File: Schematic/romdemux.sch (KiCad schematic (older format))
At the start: 14 parts, among them SW10 SW_Push, U10 27C020, U11 74LS154, U12 NE555

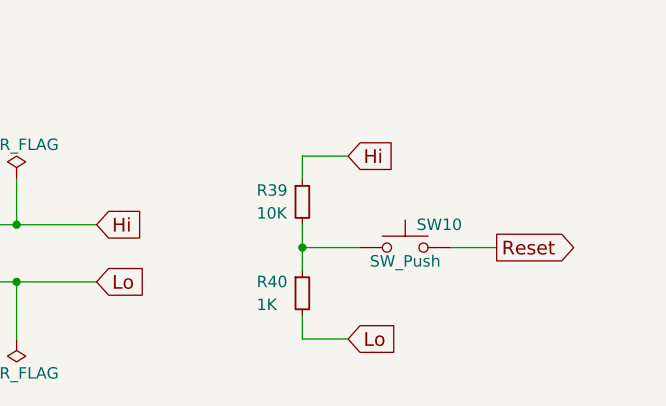
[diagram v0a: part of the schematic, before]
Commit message: Fixed up the reset line circuitry
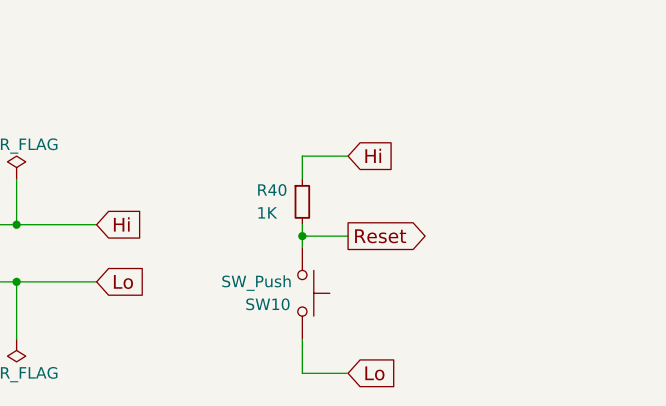
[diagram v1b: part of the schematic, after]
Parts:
- removed R39: 10K, Resistor_THT:R_Axial_DIN0204_L3.6mm_D1.6mm_P1.90mm_Vertical, symbol ttt_ttl-rescue:R_Small
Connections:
- wire segments 85 -> 84
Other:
- moved on the sheet: R40, SW10
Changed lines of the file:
@@
 L ttt_ttl-rescue:SW_Push SW10
 U 1 1 5CF8072E
-P 5700 7000
-F 0 "SW10" H 5750 7100 50  0000 L CNN
-F 1 "SW_Push" H 5700 6940 50  0000 C CNN
-F 2 "Button_Switch_THT:SW_PUSH_6mm_H8mm" H 5700 7200 50  0001 C CNN
-F 3 "" H 5700 7200 50  0001 C CNN
-	1    5700 7000
-	1    0    0    -1
-$EndComp
-Text GLabel 6100 7000 2    60   Output ~ 0
+P 5250 7200
+F 0 "SW10" V 5300 6950 50  0000 L CNN
+F 1 "SW_Push" V 5200 7000 50  0000 C CNN
+F 2 "Button_Switch_THT:SW_PUSH_6mm_H8mm" H 5250 7400 50  0001 C CNN
+F 3 "" H 5250 7400 50  0001 C CNN
+	1    5250 7200
+	0    1    1    0
+$EndComp
+Text GLabel 5450 6950 2    60   Output ~ 0
 Reset
 Wire Wire Line
-	5900 7000 6100 7000
-$Comp
-L ttt_ttl-rescue:R_Small R39
-U 1 1 5CF80923
+	5250 6950 5450 6950
+$Comp
+L ttt_ttl-rescue:R_Small R40
+U 1 1 5CF80CCF
 P 5250 6800
-F 0 "R39" H 5050 6850 50  0000 L CNN
-F 1 "10K" H 5050 6750 50  0000 L CNN
+F 0 "R40" H 5050 6850 50  0000 L CNN
+F 1 "1K" H 5050 6750 50  0000 L CNN
 F 2 "Resistor_THT:R_Axial_DIN0204_L3.6mm_D1.6mm_P1.90mm_Vertical" H 5250 6800 50  0001 C CNN
 F 3 "" H 5250 6800 50  0001 C CNN
@@
 	1    0    0    -1
 $EndComp
-$Comp
-L ttt_ttl-rescue:R_Small R40
-U 1 1 5CF80CCF
-P 5250 7200
-F 0 "R40" H 5050 7250 50  0000 L CNN
-F 1 "1K" H 5050 7150 50  0000 L CNN
-F 2 "Resistor_THT:R_Axial_DIN0204_L3.6mm_D1.6mm_P1.90mm_Vertical" H 5250 7200 50  0001 C CNN
-F 3 "" H 5250 7200 50  0001 C CNN
-	1    5250 7200
-	1    0    0    -1
-$EndComp
-Wire Wire Line
-	5250 7100 5250 7000
-Wire Wire Line
-	5500 7000 5250 7000
-Connection ~ 5250 7000
-Text GLabel 5450 7400 2    60   Input ~ 0
+Text GLabel 5450 7550 2    60   Input ~ 0
 Lo
 Text GLabel 5450 6600 2    60   Input ~ 0
@@
 	5250 6600 5250 6700
 Wire Wire Line
-	5450 7400 5250 7400
-Wire Wire Line
-	5250 7400 5250 7300
+	5450 7550 5250 7550
 Wire Wire Line
 	3200 2050 3550 2050
@@
 Wire Wire Line
 	4000 7150 4350 7150
-Wire Wire Line
-	5250 7000 5250 6900
 $Comp
 L Timer:NE555 U12
@@
 	1    0    0    -1
 $EndComp
+Wire Wire Line
+	5250 6900 5250 6950
+Wire Wire Line
+	5250 7400 5250 7550
+Connection ~ 5250 6950
+Wire Wire Line
+	5250 6950 5250 7000
 $EndSCHEMATC

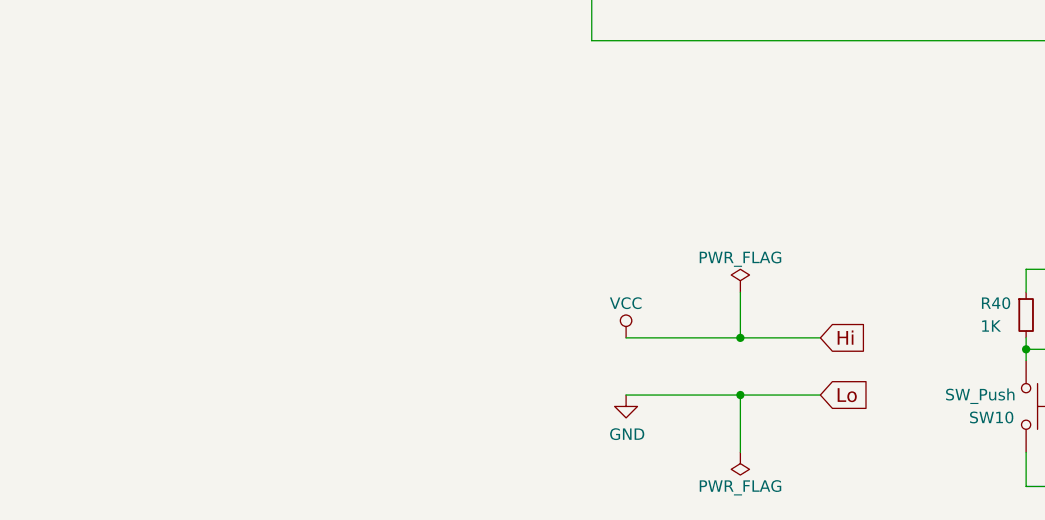
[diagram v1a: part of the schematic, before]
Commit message: Updated the schematic and PCB with the new flip-flip pinouts and footprints.
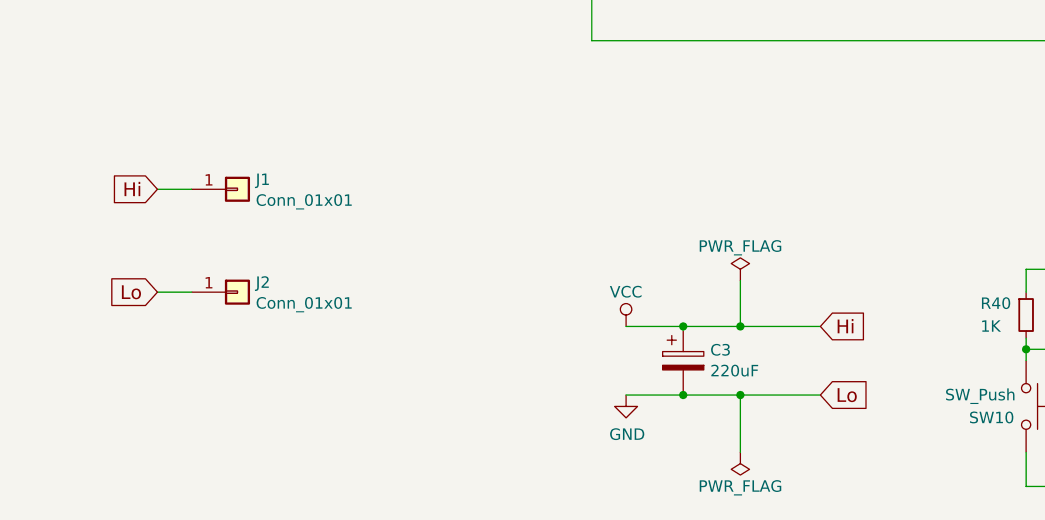
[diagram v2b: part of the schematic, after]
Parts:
- added C3: 220uF, Capacitor_THT:CP_Radial_D10.0mm_P2.50mm, symbol Device:CP
- added J1, J2: Conn_01x01, Connector_Pin:Pin_D1.0mm_L10.0mm, symbol Connector_Generic:Conn_01x01
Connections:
- wire segments 84 -> 88
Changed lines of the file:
@@
 L power:VCC #PWR02
 U 1 1 5CF78A19
-P 3500 6900
-F 0 "#PWR02" H 3500 6750 50  0001 C CNN
-F 1 "VCC" H 3500 7050 50  0000 C CNN
-F 2 "" H 3500 6900 50  0001 C CNN
-F 3 "" H 3500 6900 50  0001 C CNN
-	1    3500 6900
-	1    0    0    -1
-$EndComp
-Text GLabel 4350 6900 2    60   Input ~ 0
+P 3500 6850
+F 0 "#PWR02" H 3500 6700 50  0001 C CNN
+F 1 "VCC" H 3500 7000 50  0000 C CNN
+F 2 "" H 3500 6850 50  0001 C CNN
+F 3 "" H 3500 6850 50  0001 C CNN
+	1    3500 6850
+	1    0    0    -1
+$EndComp
+Text GLabel 4350 6850 2    60   Input ~ 0
 Hi
 Text GLabel 4350 7150 2    60   Input ~ 0
@@
 Move8
 Wire Wire Line
-	3500 6900 4000 6900
-Wire Wire Line
-	3500 7150 4000 7150
+	3500 6850 3750 6850
+Wire Wire Line
+	3500 7150 3750 7150
 Wire Wire Line
 	6100 1050 6300 1050
@@
 L power:PWR_FLAG #FLG03
 U 1 1 5CF7F449
-P 4000 6700
-F 0 "#FLG03" H 4000 6775 50  0001 C CNN
-F 1 "PWR_FLAG" H 4000 6850 50  0000 C CNN
-F 2 "" H 4000 6700 50  0001 C CNN
-F 3 "" H 4000 6700 50  0001 C CNN
-	1    4000 6700
+P 4000 6650
+F 0 "#FLG03" H 4000 6725 50  0001 C CNN
+F 1 "PWR_FLAG" H 4000 6800 50  0000 C CNN
+F 2 "" H 4000 6650 50  0001 C CNN
+F 3 "" H 4000 6650 50  0001 C CNN
+	1    4000 6650
 	1    0    0    -1
 $EndComp
@@
 $EndComp
 Wire Wire Line
-	4000 6700 4000 6900
-Connection ~ 4000 6900
+	4000 6650 4000 6850
+Connection ~ 4000 6850
 Wire Wire Line
 	4000 7400 4000 7150
@@
 	3200 2050 3550 2050
 Wire Wire Line
-	4000 6900 4350 6900
+	4000 6850 4350 6850
 Wire Wire Line
 	4000 7150 4350 7150
@@
 Wire Wire Line
 	5250 6950 5250 7000
+$Comp
+L Device:CP C3
+U 1 1 5D0C87CD
+P 3750 7000
+F 0 "C3" H 3868 7046 50  0000 L CNN
+F 1 "220uF" H 3868 6955 50  0000 L CNN
+F 2 "Capacitor_THT:CP_Radial_D10.0mm_P2.50mm" H 3788 6850 50  0001 C CNN
+F 3 "~" H 3750 7000 50  0001 C CNN
+	1    3750 7000
+	1    0    0    -1
+$EndComp
+Connection ~ 3750 6850
+Wire Wire Line
+	3750 6850 4000 6850
+Connection ~ 3750 7150
+Wire Wire Line
+	3750 7150 4000 7150
+Text GLabel 1450 6250 0    60   Input ~ 0
+Hi
+Text GLabel 1450 6700 0    60   Input ~ 0
+Lo
+Wire Wire Line
+	1450 6250 1600 6250
+Wire Wire Line
+	1450 6700 1600 6700
+$Comp
+L Connector_Generic:Conn_01x01 J1
+U 1 1 5D008CFB
+P 1800 6250
+F 0 "J1" H 1880 6292 50  0000 L CNN
+F 1 "Conn_01x01" H 1880 6201 50  0000 L CNN
+F 2 "Connector_Pin:Pin_D1.0mm_L10.0mm" H 1800 6250 50  0001 C CNN
+F 3 "~" H 1800 6250 50  0001 C CNN
+	1    1800 6250
+	1    0    0    -1
+$EndComp
+$Comp
+L Connector_Generic:Conn_01x01 J2
+U 1 1 5D00904C
+P 1800 6700
+F 0 "J2" H 1880 6742 50  0000 L CNN
+F 1 "Conn_01x01" H 1880 6651 50  0000 L CNN
+F 2 "Connector_Pin:Pin_D1.0mm_L10.0mm" H 1800 6700 50  0001 C CNN
+F 3 "~" H 1800 6700 50  0001 C CNN
+	1    1800 6700
+	1    0    0    -1
+$EndComp
 $EndSCHEMATC

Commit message: Fixed ROM part, was 27C020, should be 27C2001
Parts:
- U10: value 27C020 -> 27C2001; symbol ttt_ttl-rescue:27C020 -> ttt_ttl-rescue:27C2001
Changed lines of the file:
@@
 	4550 1550 4750 1550
 $Comp
-L ttt_ttl-rescue:27C020 U10
+L ttt_ttl-rescue:27C2001 U10
 U 1 1 5CF7A49D
 P 2250 1850
@@
 AR Path="/5CF77C08/5CF7A49D" Ref="U10"  Part="1"
 F 0 "U10" H 2250 2850 50  0000 C CNN
-F 1 "27C020" H 2250 450 50  0000 C CNN
+F 1 "27C2001" H 2250 450 50  0000 C CNN
 F 2 "Package_DIP:DIP-32_W15.24mm_Socket" H 2250 1850 50  0001 C CNN
 F 3 "" H 2250 1850 50  0001 C CNN

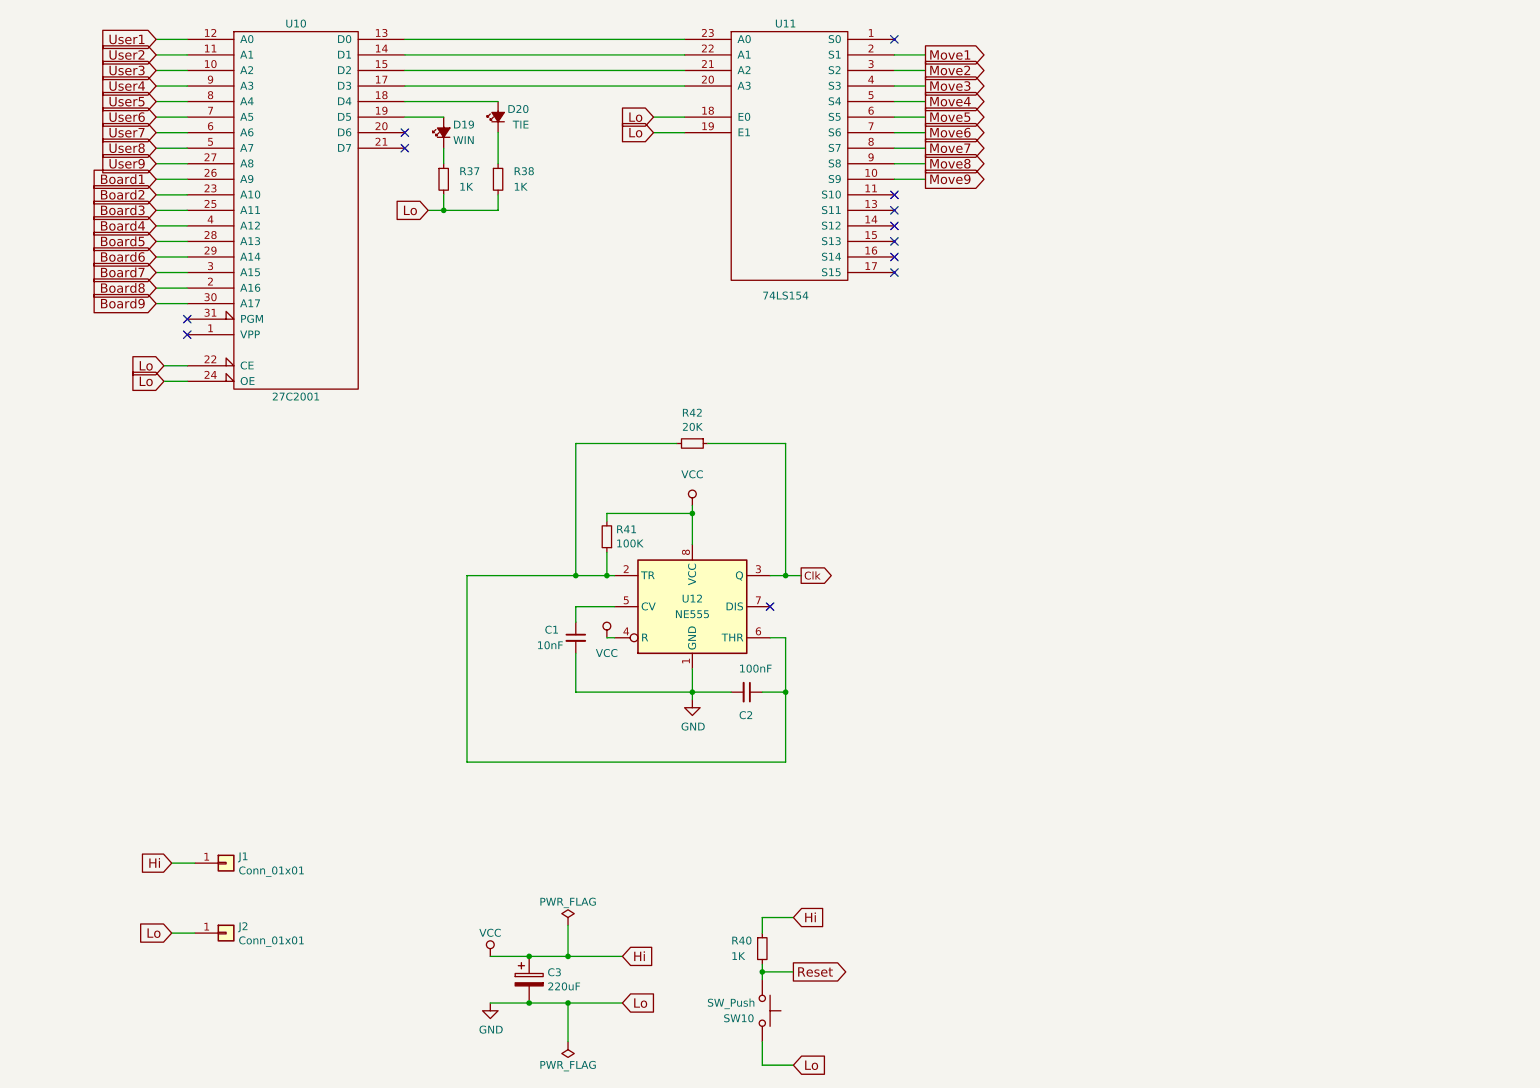
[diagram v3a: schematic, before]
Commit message: Smaller 8Kx8 EEPROM is working
I managed to get the code to generate a ROM file which uses a 4-bit board
state plus the user's moves to look up the net board move and the next
board state. I've redone the schematic, PCB and I've started on the
documentation. I need to redraw the design diagram.
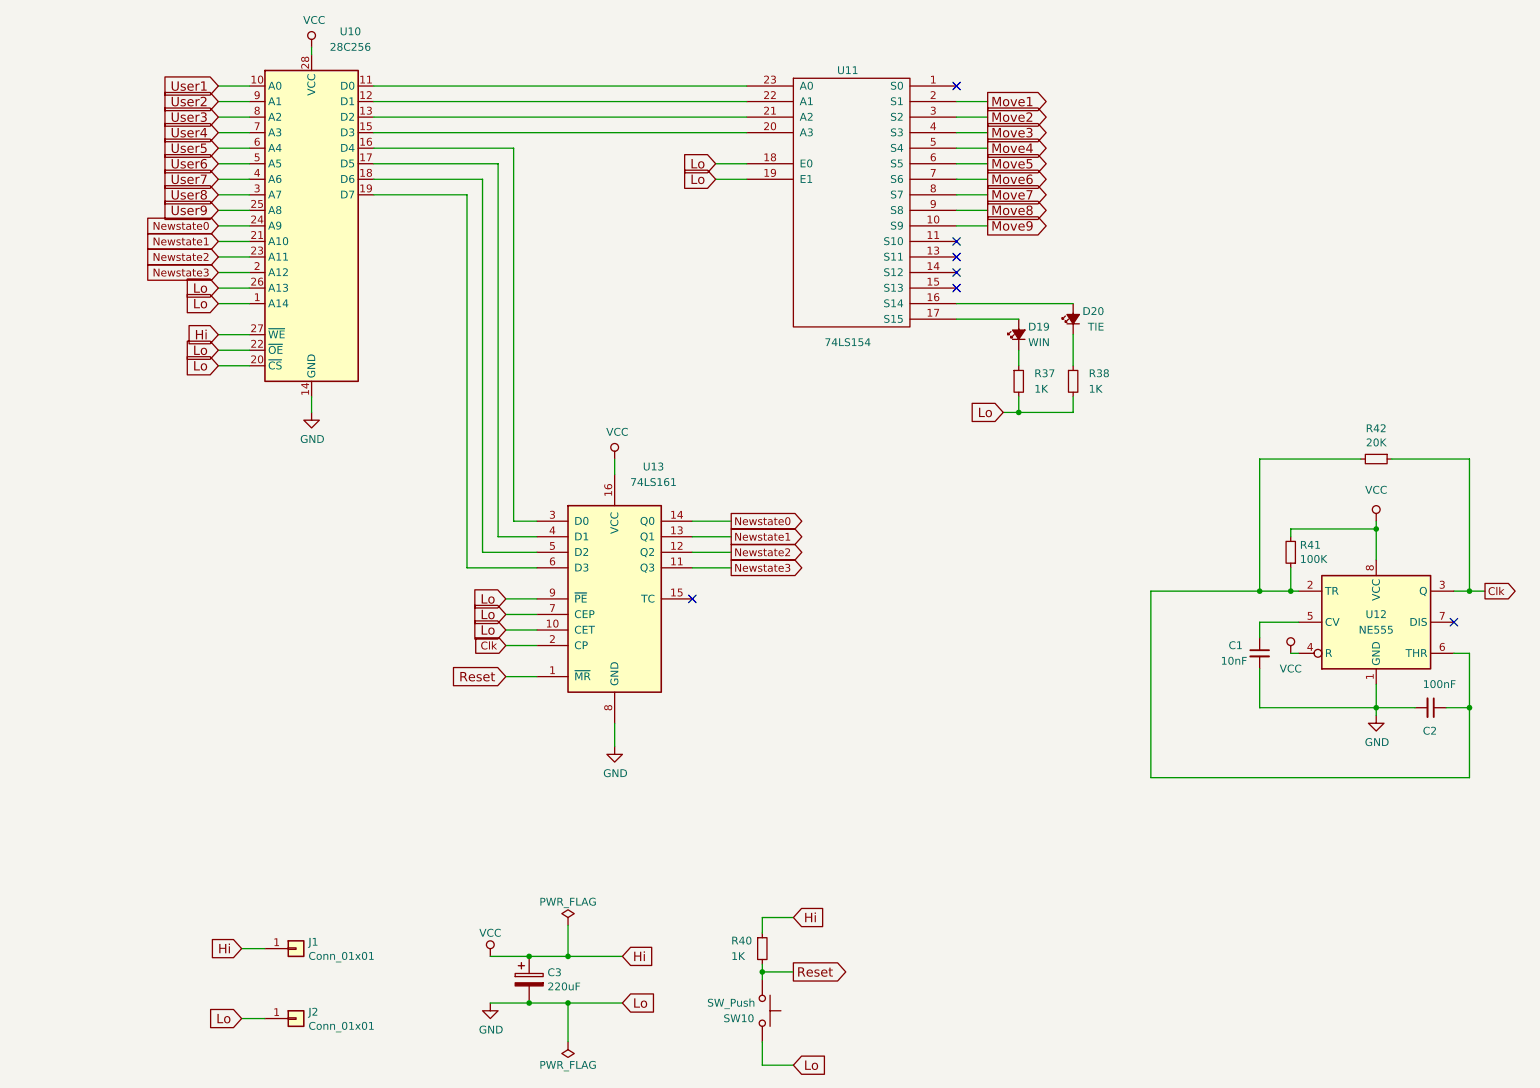
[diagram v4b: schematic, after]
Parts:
- removed U10: 27C2001, Package_DIP:DIP-32_W15.24mm_Socket, symbol ttt_ttl-rescue:27C2001
- added U10: 28C256, Package_DIP:DIP-28_W15.24mm_Socket, symbol Memory_EEPROM:28C256
- added U13: 74LS161, Package_DIP:DIP-16_W7.62mm, symbol 74xx:74LS161
- D19, D20: footprint Diode_THT:D_DO-41_SOD81_P7.62mm_Horizontal -> LED_THT:LED_D3.0mm
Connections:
- net Clk: now also U13.2 (CP)
- net GND: now also U10.1 (A14), U10.14 (GND), U10.20 (~CS), U10.22 (~OE), U10.26 (A13), U13.10 (CET), U13.7 (CEP), U13.8 (GND), U13.9 (~PE)
- net Reset: now also U13.1 (~MR)
- net User1: now also U10.10 (A0)
- net User2: now also U10.9 (A1)
- net User3: now also U10.8 (A2)
- net User4: now also U10.7 (A3)
- net User5: now also U10.6 (A4)
- net User6: now also U10.5 (A5)
- net User7: now also U10.4 (A6)
- net User8: now also U10.3 (A7)
- net User9: now also U10.25 (A8)
- net VCC: now also U10.27 (~WE), U10.28 (VCC), U13.16 (VCC)
- net at U11.23 (A0): now also U10.11 (D0)
- net at U11.22 (A1): now also U10.12 (D1)
- net at U11.21 (A2): now also U10.13 (D2)
- net at U11.20 (A3): now also U10.15 (D3)
- net at D20.2 (A): now also U11.16 (S14)
- net at D19.2 (A): now also U11.17 (S15)
- new net: U10.16 (D4), U13.3 (D0)
- new net: U10.17 (D5), U13.4 (D1)
- new net: U10.18 (D6), U13.5 (D2)
- new net: U10.19 (D7), U13.6 (D3)
- new net Newstate0: U10.24 (A9), U13.14 (Q0)
- new net Newstate1: U10.21 (A10), U13.13 (Q1)
- new net Newstate2: U10.23 (A11), U13.12 (Q2)
- new net Newstate3: U10.2 (A12), U13.11 (Q3)
- no-connect marks 12 -> 7
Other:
- moved on the sheet: C1, C2, D19, D20, J1, J2, R37, R38, R41, R42, U11, U12

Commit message: I bought different pushbuttons, so I updated the PCB design.
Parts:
- SW10: footprint Button_Switch_THT:SW_PUSH_6mm_H8mm -> Button_Switch_THT:Push_E-Switch_KS01Q01
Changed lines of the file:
@@
 F 0 "SW10" V 5300 6950 50  0000 L CNN
 F 1 "SW_Push" V 5200 7000 50  0000 C CNN
-F 2 "Button_Switch_THT:SW_PUSH_6mm_H8mm" H 5250 7400 50  0001 C CNN
+F 2 "Button_Switch_THT:Push_E-Switch_KS01Q01" H 5250 7400 50  0001 C CNN
 F 3 "" H 5250 7400 50  0001 C CNN
 	1    5250 7200

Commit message: Small circuit change. Tie/win LEDs must connect to demux active low output.
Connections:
- net GND: no longer R37.2, R38.2
- net VCC: now also D19.2 (A), D20.2 (A)
- net at D20.1 (K): now also R38.2; no longer R38.1
- net at U11.16 (S14): now also R38.1; no longer D20.2 (A)
- net at D19.1 (K): now also R37.2; no longer R37.1
- net at U11.17 (S15): now also R37.1; no longer D19.2 (A)
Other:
- moved on the sheet: D19, D20, R37, R38
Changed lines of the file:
@@
 L ttt_ttl-rescue:LED_Small_ALT D20
 U 1 1 5CF7A612
-P 7250 2750
-F 0 "D20" V 7300 2550 50  0000 L CNN
-F 1 "TIE" V 7200 2550 50  0000 L CNN
-F 2 "LED_THT:LED_D3.0mm" V 7250 2750 50  0001 C CNN
-F 3 "" V 7250 2750 50  0001 C CNN
-	1    7250 2750
-	0    -1   -1   0
+P 7250 3150
+F 0 "D20" V 7300 2950 50  0000 L CNN
+F 1 "TIE" V 7200 2950 50  0000 L CNN
+F 2 "LED_THT:LED_D3.0mm" V 7250 3150 50  0001 C CNN
+F 3 "" V 7250 3150 50  0001 C CNN
+	1    7250 3150
+	0    1    1    0
 $EndComp
 $Comp
 L ttt_ttl-rescue:LED_Small_ALT D19
 U 1 1 5CF7A765
-P 6900 2850
-F 0 "D19" V 6950 2650 50  0000 L CNN
-F 1 "WIN" V 6850 2650 50  0000 L CNN
-F 2 "LED_THT:LED_D3.0mm" V 6900 2850 50  0001 C CNN
-F 3 "" V 6900 2850 50  0001 C CNN
-	1    6900 2850
-	0    -1   -1   0
+P 6900 3150
+F 0 "D19" V 6950 2950 50  0000 L CNN
+F 1 "WIN" V 6850 2950 50  0000 L CNN
+F 2 "LED_THT:LED_D3.0mm" V 6900 3150 50  0001 C CNN
+F 3 "" V 6900 3150 50  0001 C CNN
+	1    6900 3150
+	0    1    1    0
 $EndComp
 $Comp
 L ttt_ttl-rescue:R_Small R38
 U 1 1 5CF7A7DD
-P 7250 3150
-F 0 "R38" H 7350 3200 50  0000 L CNN
-F 1 "1K" H 7350 3100 50  0000 L CNN
-F 2 "Resistor_THT:R_Axial_DIN0204_L3.6mm_D1.6mm_P1.90mm_Vertical" H 7250 3150 50  0001 C CNN
-F 3 "" H 7250 3150 50  0001 C CNN
-	1    7250 3150
+P 7250 2750
+F 0 "R38" H 7350 2800 50  0000 L CNN
+F 1 "1K" H 7350 2700 50  0000 L CNN
+F 2 "Resistor_THT:R_Axial_DIN0204_L3.6mm_D1.6mm_P1.90mm_Vertical" H 7250 2750 50  0001 C CNN
+F 3 "" H 7250 2750 50  0001 C CNN
+	1    7250 2750
 	1    0    0    -1
 $EndComp
@@
 L ttt_ttl-rescue:R_Small R37
 U 1 1 5CF7A87F
-P 6900 3150
-F 0 "R37" H 7000 3200 50  0000 L CNN
-F 1 "1K" H 7000 3100 50  0000 L CNN
-F 2 "Resistor_THT:R_Axial_DIN0204_L3.6mm_D1.6mm_P1.90mm_Vertical" H 6900 3150 50  0001 C CNN
-F 3 "" H 6900 3150 50  0001 C CNN
-	1    6900 3150
+P 6900 2850
+F 0 "R37" H 7000 2900 50  0000 L CNN
+F 1 "1K" H 7000 2800 50  0000 L CNN
+F 2 "Resistor_THT:R_Axial_DIN0204_L3.6mm_D1.6mm_P1.90mm_Vertical" H 6900 2850 50  0001 C CNN
+F 3 "" H 6900 2850 50  0001 C CNN
+	1    6900 2850
 	1    0    0    -1
 $EndComp
@@
 Wire Wire Line
 	7250 2850 7250 3050
-Text GLabel 6800 3350 0    60   Input ~ 0
-Lo
 Wire Wire Line
 	6800 3350 6900 3350
@@
 Wire Wire Line
 	2350 3350 2350 3250
+Text GLabel 6800 3350 0    60   Input ~ 0
+Hi
 $EndSCHEMATC
